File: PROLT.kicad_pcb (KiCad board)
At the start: 4 copper layers, 80 x 80 mm, 82 parts, among them IC1 BTS4175SGA, IC2 IFX9201SGAUMA1, IC3 IFX9201SGAUMA1, J1 64334-0100, J2 USB, M1 Module:mega-mcu100/0.3, M2 Module-vr-max9924-0.1, M3 Module-power_12and5V-0.2, U1 JDY-33, U2 VNLD5160TR-E, U3 VNLD5160TR-E, U4 VNLD5160TR-E

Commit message: Rev B
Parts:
- added R17: 4.7k, Hellen:R0603, F.Cu at (155.0, 91.1)
- added R18: 4.7k, Hellen:R0603, F.Cu at (152.4, 91.2)
- added R19: 4.7k, Hellen:R0603, F.Cu at (158.2, 91.1)
- added R20: 4.7k, Hellen:R0603, F.Cu at (160.8, 91.1)
- added R21: 4.7k, Hellen:R0603, F.Cu at (146.4, 91.2)
- added R22: 4.7k, Hellen:R0603, F.Cu at (148.9, 91.2)
- C28: value 100nF -> 100n
- R5: value 10k -> 150
- R6: value 10k -> 0R
- R7: value 10k -> 15k
- moved R5 0.60 mm to (162.1, 91.1)
- moved R6 0.34 mm to (163.4, 91.0)
- moved R3 0.10 mm to (156.9, 91.1)
- moved R4 0.10 mm to (159.5, 91.1)
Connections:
- R1 pad 2: /INJ1_IN -> Net-(U2-IN1)
- R10 pad 2: /LS2 -> Net-(U4-IN2)
- R2 pad 2: /INJ2_IN -> Net-(U2-IN2)
- R3 pad 2: /INJ3_IN -> Net-(U3-IN1)
- R4 pad 2: /INJ4_IN -> Net-(U3-IN2)
- R9 pad 2: /LS1 -> Net-(U4-IN1)
- U2 pad 1: /INJ1_IN -> Net-(U2-IN1)
- U2 pad 3: /INJ2_IN -> Net-(U2-IN2)
- U3 pad 1: /INJ3_IN -> Net-(U3-IN1)
- U3 pad 3: /INJ4_IN -> Net-(U3-IN2)
- U4 pad 1: /LS1 -> Net-(U4-IN1)
- U4 pad 3: /LS2 -> Net-(U4-IN2)
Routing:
- net /INJ1_IN: track 11.8 -> 6.94 mm
- net /LS1: track 13.7 -> 8.85 mm
- net /INJ2_IN: track 12.0 -> 7.70 mm
- net Net-(U4-IN2): track 0.00 -> 4.15 mm
- net Net-(U2-IN1): track 0.00 -> 4.10 mm
- net Net-(U2-IN2): track 0.00 -> 4.03 mm
- net Net-(U3-IN2): track 0.00 -> 4.03 mm
- net Net-(U4-IN1): track 0.00 -> 4.02 mm
- net Net-(U3-IN1): track 0.00 -> 3.97 mm
- net /INJ3_IN: track 12.4 -> 8.70 mm
- net GND: track 10.8 -> 7.89 mm, vias 165 -> 162
- net /LS2: track 14.5 -> 11.9 mm
- net /INJ4_IN: track 13.2 -> 10.8 mm
- net /DC2_DIS: track 38.9 -> 37.8 mm
- net /HS: track 11.7 -> 12.6 mm
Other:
- board text added: "PROLT REV.B"
- board text removed: "PROLT REV.A"

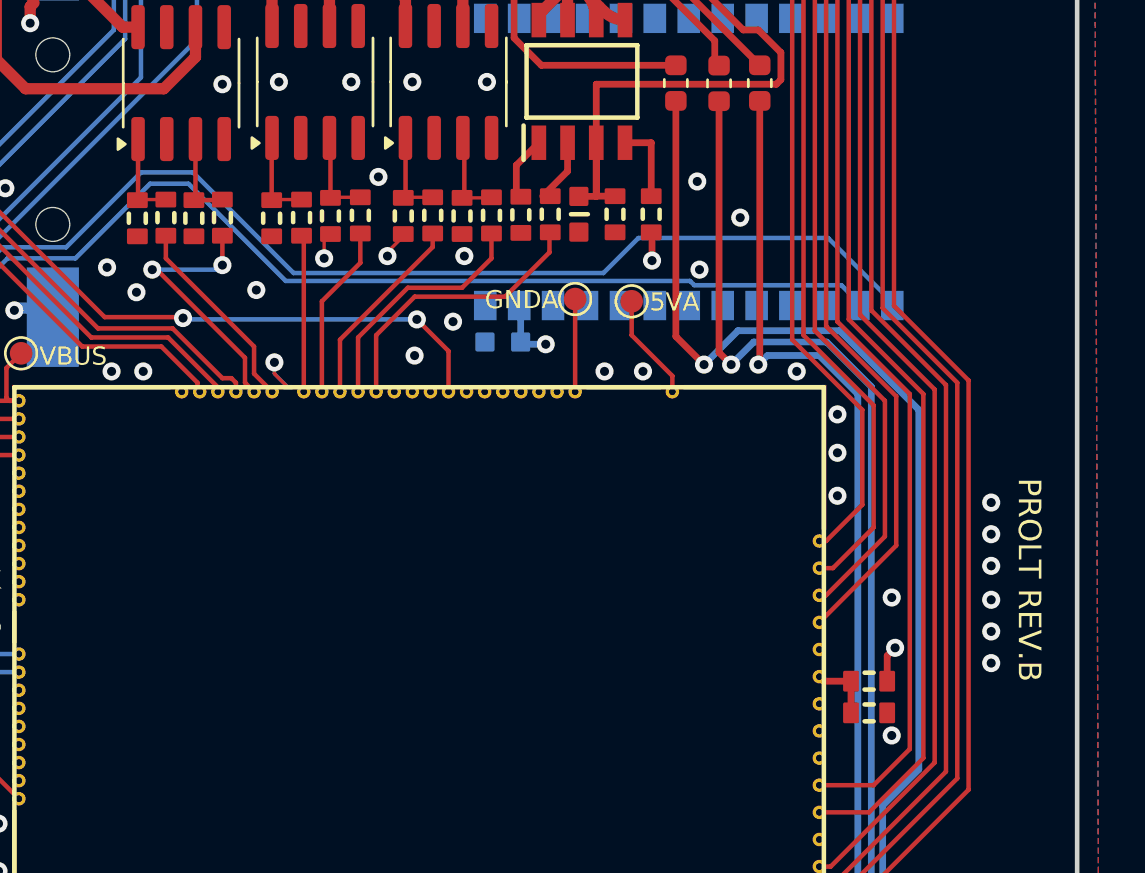
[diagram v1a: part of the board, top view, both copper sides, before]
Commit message: Stupid mistake — I ended up making a voltage divider instead of a protection circuit. I'm the best.
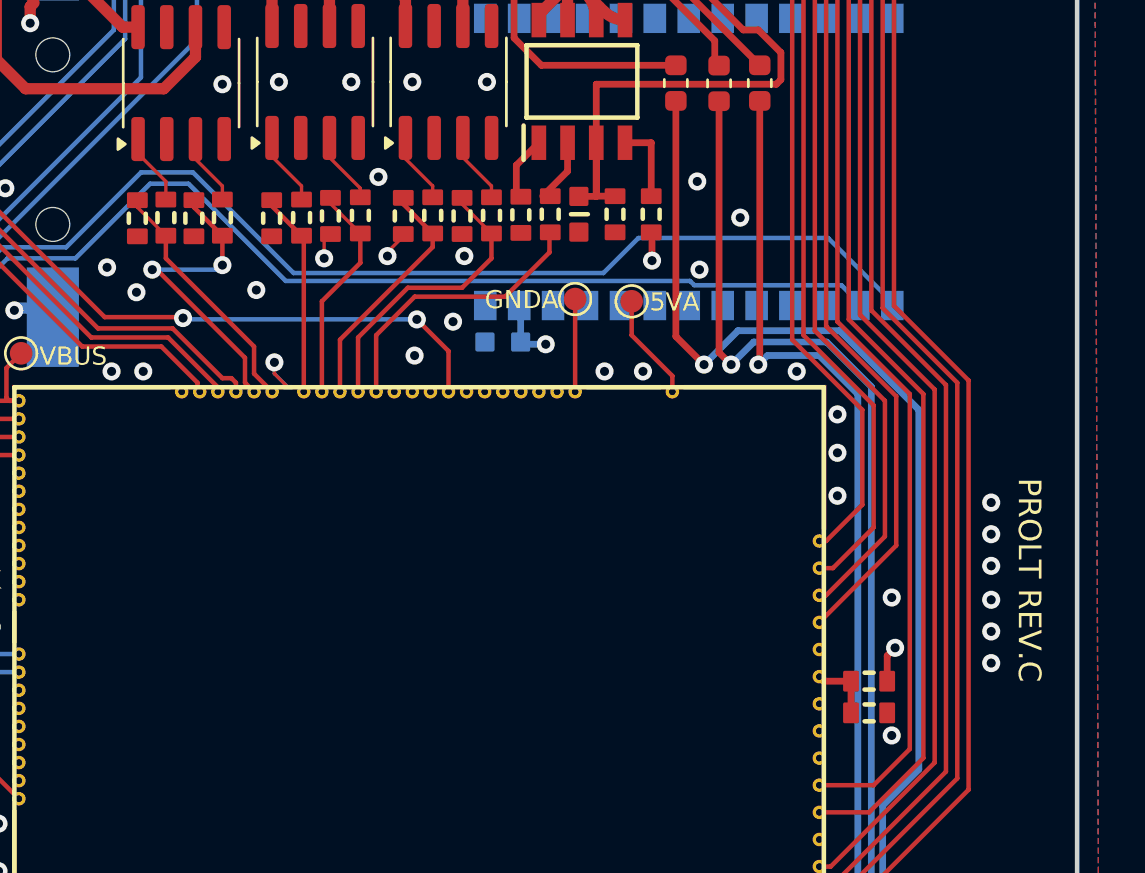
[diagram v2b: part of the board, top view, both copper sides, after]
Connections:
- R1 pad 2: Net-(U2-IN1) -> /INJ1_IN
- R10 pad 2: Net-(U4-IN2) -> /LS2
- R2 pad 2: Net-(U2-IN2) -> /INJ2_IN
- R3 pad 2: Net-(U3-IN1) -> /INJ3_IN
- R4 pad 2: Net-(U3-IN2) -> /INJ4_IN
- R9 pad 2: Net-(U4-IN1) -> /LS1
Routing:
- net /LS2: track 11.9 -> 14.1 mm
- net /LS1: track 8.85 -> 11.0 mm
- net /INJ2_IN: track 7.70 -> 9.87 mm
- net /INJ1_IN: track 6.94 -> 9.10 mm
- net /INJ3_IN: track 8.70 -> 10.8 mm
- net /INJ4_IN: track 10.8 -> 13.0 mm
- net Net-(U4-IN2): track 4.15 -> 3.20 mm
- net Net-(U3-IN1): track 3.97 -> 3.13 mm
- net Net-(U4-IN1): track 4.02 -> 3.18 mm
- net Net-(U2-IN1): track 4.10 -> 3.28 mm
- net Net-(U2-IN2): track 4.03 -> 3.24 mm
- net Net-(U3-IN2): track 4.03 -> 3.25 mm
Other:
- board text added: "PROLT REV.C"
- board text removed: "PROLT REV.B"

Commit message: Rev D
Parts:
- removed C28: 100n, Hellen:C0603
- removed R17, R18, R19, R20: 4.7k, Hellen:R0603
- removed U1: JDY-33, Hellen:JDY-33
- removed U3: VNLD5160TR-E, Package_SO:SOIC-8_3.9x4.9mm_P1.27mm
- added C29: 100n, Capacitor_SMD:C_0603_1608Metric, F.Cu at (162.3, 89.4)
- added C30: 100n, Capacitor_SMD:C_0603_1608Metric, F.Cu at (162.3, 92.7)
- added Q1: VND14NV04TR-E, Package_TO_SOT_SMD:TO-252-2, F.Cu at (153.6, 80.2)
- added Q2: VND14NV04TR-E, Package_TO_SOT_SMD:TO-252-2, F.Cu at (162.1, 80.1)
- added Q3: VND14NV04TR-E, Package_TO_SOT_SMD:TO-252-2, B.Cu at (153.6, 80.1)
- added Q4: VND14NV04TR-E, Package_TO_SOT_SMD:TO-252-2, B.Cu at (162.0, 80.1)
- R3, R4: moved to B.Cu
- U2: value VNLD5160TR-E -> SN74LVC4245APWR; footprint Package_SO:SOIC-8_3.9x4.9mm_P1.27mm -> EasyEda2Kicad:TSSOP-24_L7.8-W4.4-P0.65-LS6.4-BL
- moved G1 71.0 mm to (111.2, 61.2)
- moved TP13 16.4 mm to (182.2, 61.4)
- moved R4 8.93 mm to (166.2, 85.2), turned to -90 degrees
- moved U2 7.93 mm to (157.3, 91.9), turned to 180 degrees
- moved R2 7.13 mm to (157.8, 85.3), turned to -90 degrees
- moved R3 5.96 mm to (157.8, 85.2), turned to -90 degrees
- moved C1 3.97 mm to (168.6, 91.2)
- moved R5 3.97 mm to (166.1, 91.3)
- moved R6 3.97 mm to (167.4, 91.2)
- moved R7 3.97 mm to (171.8, 91.2)
- moved R8 3.97 mm to (170.2, 91.2)
- moved IC1 3.97 mm to (168.8, 85.4)
- moved R1 3.93 mm to (151.3, 87.3), turned to 0 degrees
- moved F2 3.44 mm to (174.3, 85.3)
- moved F3 3.44 mm to (176.1, 85.3)
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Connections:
- M1 pad N13: Net-(M1-UART2_TX_(PD5)) -> unconnected-(M1-UART2_TX_(PD5)-PadN13)
- M1 pad N14: Net-(M1-UART2_RX_(PD6)) -> unconnected-(M1-UART2_RX_(PD6)-PadN14)
- R1 pad 2: /INJ1_IN -> /Injectors/OUT_5V_1
- R2 pad 2: /INJ2_IN -> /Injectors/OUT_5V_2
- R3 pad 2: /INJ3_IN -> /Injectors/OUT_5V_3
- R4 pad 2: /INJ4_IN -> /Injectors/OUT_5V_4
- U2 pad 1: Net-(U2-IN1) -> +5VA
- U2 pad 2: unconnected-(U2-STATUS1-Pad2) -> GND
- U2 pad 3: Net-(U2-IN2) -> /Injectors/OUT_5V_4
- U2 pad 4: unconnected-(U2-STATUS2-Pad4) -> /Injectors/OUT_5V_3
- U2 pad 5: GND -> /Injectors/OUT_5V_2
- U2 pad 6: /INJ2_OUT -> /Injectors/OUT_5V_1
- U2 pad 7: GND -> unconnected-(U2-A5-Pad7)
- U2 pad 8: /INJ1_OUT -> unconnected-(U2-A6-Pad8)
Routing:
- net Net-(M1-UART2_RX_(PD6)): track 66.4 -> 0.00 mm
- net Net-(M1-UART2_TX_(PD5)): track 61.6 -> 0.00 mm
- net /Injectors/OUT_5V_3: track 0.00 -> 12.8 mm, vias 0 -> 1
- net /TACH: track 46.3 -> 36.6 mm, vias 0 -> 2
- net /Injectors/OUT_5V_1: track 0.00 -> 9.15 mm
- net /Injectors/OUT_5V_4: track 0.00 -> 9.03 mm, vias 0 -> 1
- net /INJ3_OUT: track 14.1 -> 6.46 mm
- net /INJ4_IN: track 13.0 -> 6.07 mm
- net +5VA: track 75.2 -> 81.3 mm, vias 0 -> 1
- net /Injectors/OUT_5V_2: track 0.00 -> 5.38 mm
- net /INJ3_IN: track 10.8 -> 6.29 mm
- net /IGN2_OUT: track 22.1 -> 26.3 mm
- net /OUT_1: track 14.1 -> 9.96 mm
- net +3.3V: track 185.2 -> 189.2 mm
- net /IGN3_OUT: track 25.2 -> 29.2 mm
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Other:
- board text added: "PROLT REV.D"
- board text removed: "PROLT REV.C"

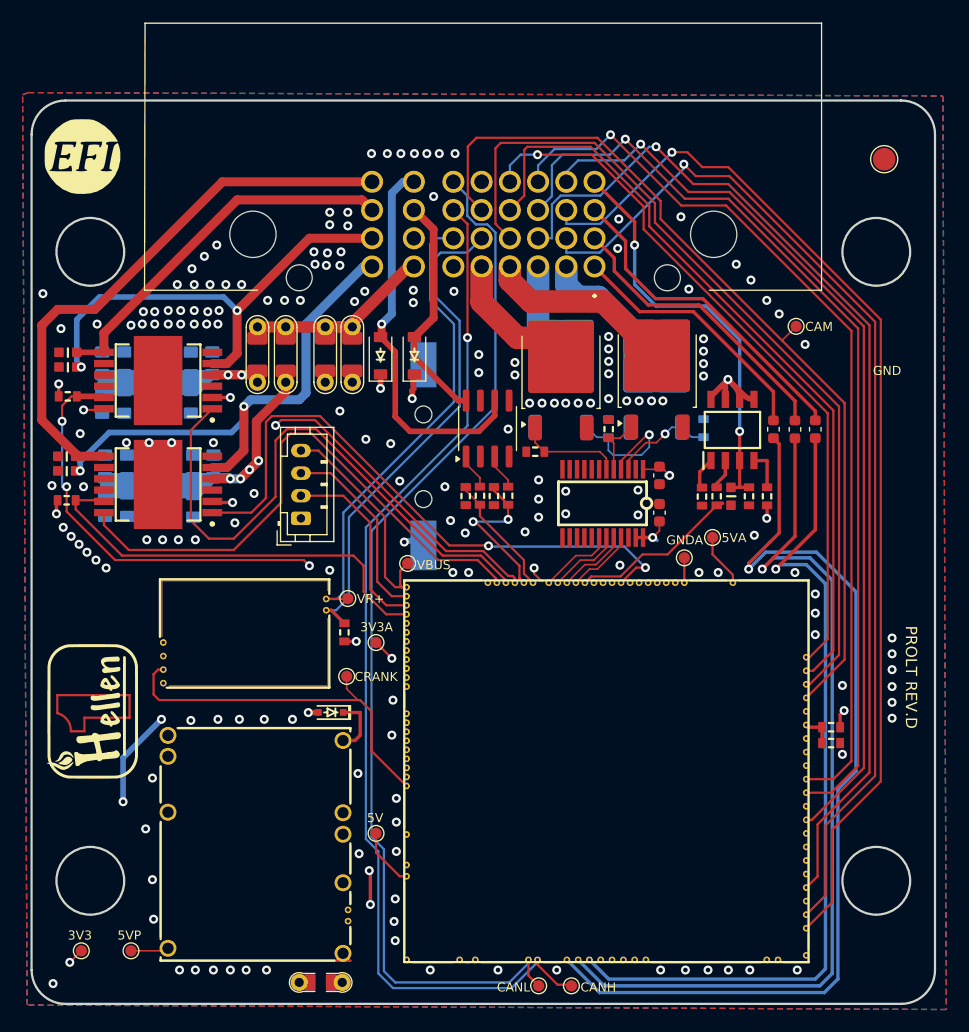
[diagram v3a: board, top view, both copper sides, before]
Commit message: Rev E
Back to VNLD5160TR-E, 1 channel per injector now
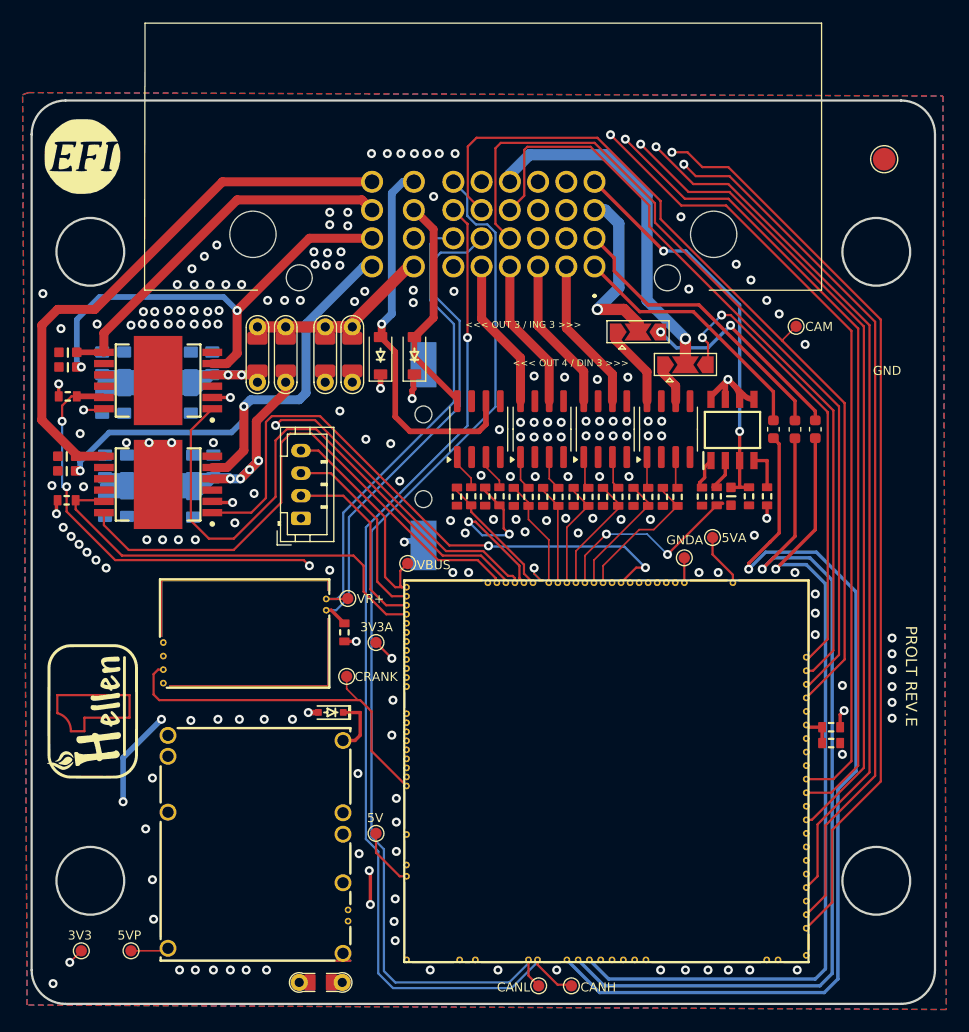
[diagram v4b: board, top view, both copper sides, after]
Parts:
- removed C29, C30: 100n, Capacitor_SMD:C_0603_1608Metric
- removed Q1, Q2, Q3, Q4: VND14NV04TR-E, Package_TO_SOT_SMD:TO-252-2
- added JP1: OUT 3 SELECTOR, Jumper:SolderJumper-3_P2.0mm_Open_TrianglePad1.0x1.5mm, F.Cu at (160.4, 76.7)
- added JP2: OUT 4 SELECTOR, Jumper:SolderJumper-3_P2.0mm_Open_TrianglePad1.0x1.5mm, F.Cu at (164.6, 79.6)
- added R17: 4.7k, Hellen:R0603, F.Cu at (154.7, 91.3)
- added R18: 4.7k, Hellen:R0603, F.Cu at (157.3, 91.3)
- added R19: 4.7k, Hellen:R0603, F.Cu at (156.0, 91.3)
- added R20: 4.7k, Hellen:R0603, F.Cu at (158.6, 91.3)
- added R23: 4.7k, Hellen:R0603, F.Cu at (160.0, 91.3)
- added R24: 4.7k, Hellen:R0603, F.Cu at (162.6, 91.3)
- added R25: 4.7k, Hellen:R0603, F.Cu at (161.3, 91.3)
- added R26: 4.7k, Hellen:R0603, F.Cu at (163.9, 91.3)
- added U1: VNLD5160TR-E, Package_SO:SOIC-8_3.9x4.9mm_P1.27mm, F.Cu at (151.9, 85.3)
- added U3: VNLD5160TR-E, Package_SO:SOIC-8_3.9x4.9mm_P1.27mm, F.Cu at (163.1, 85.3)
- R3, R4: moved to F.Cu
- U2: value SN74LVC4245APWR -> VNLD5160TR-E; footprint EasyEda2Kicad:TSSOP-24_L7.8-W4.4-P0.65-LS6.4-BL -> Package_SO:SOIC-8_3.9x4.9mm_P1.27mm
- moved R4 14.2 mm to (153.3, 91.3)
- moved R3 9.33 mm to (150.7, 91.3)
- moved R2 8.35 mm to (152.0, 91.3), turned to 90 degrees
- moved U2 6.58 mm to (157.5, 85.3), turned to 90 degrees
- moved R1 4.43 mm to (149.4, 91.3), turned to 90 degrees
- moved R21 0.78 mm to (145.6, 91.2)
- moved R22 0.78 mm to (148.1, 91.2)
- moved R10 0.78 mm to (146.9, 91.3)
- moved R9 0.78 mm to (144.4, 91.3)
- moved U4 0.78 mm to (146.3, 85.3)
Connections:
- D1 pad 2: /OUT_2 -> /OUT_1
- D2 pad 2: /OUT_3 -> /OUT_2
- J1 pad A3: /IGN3_OUT -> Net-(JP1-C)
- J1 pad B1: /OUT_1 -> /INJ4_OUT
- J1 pad D4: /IN_D3 -> Net-(JP2-C)
- J1 pad G3: /OUT_2 -> /OUT_1
- J1 pad G4: /OUT_3 -> /OUT_2
- M1 pad E11: unconnected-(M1-OUT_INJ7_(PD15)-PadE11) -> /LowSide Outputs/IN_4
- M1 pad E12: unconnected-(M1-OUT_INJ6_(PA8)-PadE12) -> /LowSide Outputs/IN_3
- R1 pad 2: /Injectors/OUT_5V_1 -> /INJ1_IN
- R2 pad 2: /Injectors/OUT_5V_2 -> /INJ2_IN
- R3 pad 1: GND -> Net-(U1-IN1)
- R3 pad 2: /Injectors/OUT_5V_3 -> /INJ1_IN
- R4 pad 1: GND -> Net-(U1-IN2)
- R4 pad 2: /Injectors/OUT_5V_4 -> /INJ2_IN
- U2 pad 1: +5VA -> Net-(U2-IN1)
- U2 pad 2: GND -> unconnected-(U2-STATUS1-Pad2)
- U2 pad 3: /Injectors/OUT_5V_4 -> Net-(U2-IN2)
- U2 pad 4: /Injectors/OUT_5V_3 -> unconnected-(U2-STATUS2-Pad4)
- U2 pad 5: /Injectors/OUT_5V_2 -> GND
- U2 pad 6: /Injectors/OUT_5V_1 -> /INJ4_OUT
- U2 pad 7: unconnected-(U2-A5-Pad7) -> GND
- U2 pad 8: unconnected-(U2-A6-Pad8) -> /INJ3_OUT
- U4 pad 6: /OUT_3 -> /OUT_2
- U4 pad 8: /OUT_2 -> /OUT_1
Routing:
- net +3.3VA: track 48.6 -> 13.4 mm, vias 3 -> 1
- net Net-(JP2-C): track 0.00 -> 31.4 mm, vias 0 -> 1
- net /OUT_3: track 34.4 -> 7.28 mm, vias 1 -> 0
- net /IN_D3: track 63.2 -> 40.9 mm, vias 1 -> 2
- net Net-(JP1-C): track 0.00 -> 15.9 mm, vias 0 -> 1
- net /INJ4_OUT: track 0.00 -> 13.6 mm
- net /OUT_2: track 20.6 -> 34.0 mm, vias 0 -> 1
- net /Injectors/OUT_5V_3: track 12.8 -> 0.00 mm, vias 1 -> 0
- net /LowSide Outputs/IN_4: track 0.00 -> 12.4 mm
- net /LowSide Outputs/IN_3: track 0.00 -> 10.9 mm
- net /IGN3_OUT: track 29.2 -> 19.1 mm, vias 0 -> 2
- net /OUT_1: track 9.96 -> 20.0 mm
- net /Injectors/OUT_5V_1: track 9.15 -> 0.00 mm
- net /Injectors/OUT_5V_4: track 9.03 -> 0.00 mm, vias 1 -> 0
- net /INJ3_OUT: track 6.46 -> 13.6 mm
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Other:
- board text added: "<<< OUT 3 / ING 3 >>>"
- board text added: "<<< OUT 4 / DIN 3 >>>"
- board text added: "PROLT REV.E"
- board text removed: "PROLT REV.D"
